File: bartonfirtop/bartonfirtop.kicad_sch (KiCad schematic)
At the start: 23 parts, among them J1 12v Supply, J10 LED8, J11 LED9, J12 LED10, J13 LED11, J14 LED12, J15 LED13, J16 LED14, J17 LED15, J18 LED16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

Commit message: I got a sequence working
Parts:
- added R1: 10k, symbol Device:R
- J19: symbol Connector:Conn_01x03_Pin -> Connector:Conn_01x02_Pin
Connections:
- net GND: no longer J19.2 (Pin_2)
- net at J19.1 (Pin_1), U4.19 (D34): now also R1.2
- net at U4.20 (D35): now also J19.2 (Pin_2); no longer J19.3 (Pin_3)
- net at U1.7 (VCC), U4.1 (3v3): now also R1.1
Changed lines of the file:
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@@
+	)
+	(junction
+		(at 167.64 204.47)
+		(diameter 0)
+		(color 0 0 0 0)
 	)
 	(junction
@@
 	)
 	(junction
+		(at 167.64 67.31)
+		(diameter 0)
+		(color 0 0 0 0)
+	)
+	(junction
 		(at 267.97 87.63)
 		(diameter 0)
@@
 	(wire
 		(pts
-			(xy 256.54 92.71) (xy 246.38 92.71)
+			(xy 255.27 92.71) (xy 246.38 92.71)
 		)
 		(stroke
@@
 	(wire
 		(pts
-			(xy 256.54 208.28) (xy 256.54 92.71)
+			(xy 255.27 207.01) (xy 255.27 92.71)
 		)
 		(stroke
@@
 	(wire
 		(pts
+			(xy 167.64 67.31) (xy 167.64 184.15)
+		)
+		(stroke
+			(width 0)
+			(type default)
+		)
+	)
+	(wire
+		(pts
 			(xy 135.89 158.75) (xy 53.34 158.75)
 		)
@@
 	(wire
 		(pts
+			(xy 167.64 67.31) (xy 133.35 67.31)
+		)
+		(stroke
+			(width 0)
+			(type default)
+		)
+	)
+	(wire
+		(pts
 			(xy 146.05 72.39) (xy 146.05 139.7)
 		)
@@
 	(wire
 		(pts
-			(xy 190.5 208.28) (xy 256.54 208.28)
-		)
-		(stroke
-			(width 0)
-			(type default)
-		)
-	)
-	(wire
-		(pts
 			(xy 278.13 115.57) (xy 267.97 115.57)
 		)
@@
 	(wire
 		(pts
+			(xy 167.64 204.47) (xy 252.73 204.47)
+		)
+		(stroke
+			(width 0)
+			(type default)
+		)
+	)
+	(wire
+		(pts
 			(xy 135.89 113.03) (xy 124.46 113.03)
 		)
@@
 	(wire
 		(pts
-			(xy 190.5 205.74) (xy 267.97 205.74)
-		)
-		(stroke
-			(width 0)
-			(type default)
-		)
-	)
-	(wire
-		(pts
 			(xy 278.13 181.61) (xy 194.31 181.61)
 		)
@@
 	(wire
 		(pts
+			(xy 167.64 191.77) (xy 167.64 204.47)
+		)
+		(stroke
+			(width 0)
+			(type default)
+		)
+	)
+	(wire
+		(pts
 			(xy 127 55.88) (xy 205.74 55.88)
 		)
@@
 	(wire
 		(pts
-			(xy 218.44 67.31) (xy 133.35 67.31)
+			(xy 218.44 67.31) (xy 167.64 67.31)
 		)
 		(stroke
@@
 	(wire
 		(pts
-			(xy 190.5 203.2) (xy 252.73 203.2)
+			(xy 148.59 204.47) (xy 167.64 204.47)
 		)
 		(stroke
@@
 	(wire
 		(pts
-			(xy 267.97 205.74) (xy 267.97 189.23)
+			(xy 267.97 207.01) (xy 267.97 189.23)
 		)
 		(stroke
@@
 	(wire
 		(pts
+			(xy 148.59 207.01) (xy 255.27 207.01)
+		)
+		(stroke
+			(width 0)
+			(type default)
+		)
+	)
+	(wire
+		(pts
 			(xy 267.97 167.64) (xy 267.97 157.48)
 		)
@@
 	(wire
 		(pts
-			(xy 252.73 203.2) (xy 252.73 95.25)
+			(xy 252.73 204.47) (xy 252.73 95.25)
 		)
 		(stroke
@@
 	)
 	(symbol
-		(lib_id "Connector:Conn_01x03_Pin")
-		(at 185.42 205.74 0)
+		(lib_id "Connector:Conn_01x02_Pin")
+		(at 143.51 204.47 0)
 		(unit 1)
 		(exclude_from_sim no)
@@
 		(fields_autoplaced yes)
 		(property "Reference" "J19"
-			(at 186.055 198.12 0)
+			(at 144.145 199.39 0)
 			(effects
 				(font
@@
 		)
 		(property "Value" "AB Switch"
-			(at 186.055 200.66 0)
+			(at 144.145 201.93 0)
 			(effects
 				(font
@@
 		)
 		(property "Footprint" "Connector_Molex:Molex_KK-254_AE-6410-03A_1x03_P2.54mm_Vertical"
-			(at 185.42 205.74 0)
+			(at 143.51 204.47 0)
 			(effects
 				(font
@@
 		)
 		(property "Datasheet" "~"
-			(at 185.42 205.74 0)
-			(effects
-				(font
-					(size 1.27 1.27)
-				)
-				(hide yes)
-			)
-		)
-		(property "Description" "Generic connector, single row, 01x03, script generated"
-			(at 185.42 205.74 0)
-			(effects
-				(font
-					(size 1.27 1.27)
-				)
-				(hide yes)
-			)
-		)
-		(pin "3"
+			(at 143.51 204.47 0)
+			(effects
+				(font
+					(size 1.27 1.27)
+				)
+				(hide yes)
+			)
+		)
+		(property "Description" "Generic connector, single row, 01x02, script generated"
+			(at 143.51 204.47 0)
+			(effects
+				(font
+					(size 1.27 1.27)
+				)
+				(hide yes)
+			)
 		)
 		(pin "1"
@@
 					(unit 1)
 				)
+			)
+		)
+	)
+	(symbol
+		(lib_id "Device:R")
+		(at 167.64 187.96 0)
+		(unit 1)
+		(exclude_from_sim no)
+		(in_bom yes)
+		(on_board yes)
+		(dnp no)
+		(fields_autoplaced yes)
+		(property "Reference" "R1"
+			(at 170.18 186.6899 0)
+			(effects
+				(font
+					(size 1.27 1.27)
+				)
+				(justify left)
+			)
+		)
+		(property "Value" "10k"
+			(at 170.18 189.2299 0)
+			(effects
+				(font
+					(size 1.27 1.27)
+				)
+				(justify left)
+			)
+		)
+		(property "Footprint" ""
+			(at 165.862 187.96 90)
+			(effects
+				(font
+					(size 1.27 1.27)
+				)
+				(hide yes)
+			)
+		)
+		(property "Datasheet" "~"
+			(at 167.64 187.96 0)
+			(effects
+				(font
+					(size 1.27 1.27)
+				)
+				(hide yes)
+			)
+		)
+		(property "Description" "Resistor"
+			(at 167.64 187.96 0)
+			(effects
+				(font
+					(size 1.27 1.27)
+				)
+				(hide yes)
+			)
+		)
+		(pin "1"
+		)
+		(pin "2"
+		)
+		(instances
+			(project "bartonfirtop"
+				(path "/65a05cb8-989d-4b97-b9f4-4e60970e6e14"
+					(reference "R1")
+					(unit 1)
+				)

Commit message: schematic change
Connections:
- net GND: now also J19.2 (Pin_2)
- net at U4.20 (D35): no longer J19.2 (Pin_2)
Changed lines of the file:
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@@
-	(wire
-		(pts
-			(xy 255.27 92.71) (xy 246.38 92.71)
-		)
-		(stroke
-			(width 0)
-			(type default)
-		)
-	)
 	(wire
 		(pts
@@
 	(wire
 		(pts
-			(xy 255.27 207.01) (xy 255.27 92.71)
-		)
-		(stroke
-			(width 0)
-			(type default)
-		)
-	)
-	(wire
-		(pts
 			(xy 278.13 137.16) (xy 267.97 137.16)
 		)
@@
 	(wire
 		(pts
+			(xy 148.59 207.01) (xy 267.97 207.01)
+		)
+		(stroke
+			(width 0)
+			(type default)
+		)
+	)
+	(wire
+		(pts
 			(xy 267.97 115.57) (xy 267.97 105.41)
 		)
@@
 		)
 		(stroke
-			(width 0)
-			(type default)
-		)
-	)
-	(wire
-		(pts
-			(xy 148.59 207.01) (xy 255.27 207.01)
-		)
-		(stroke

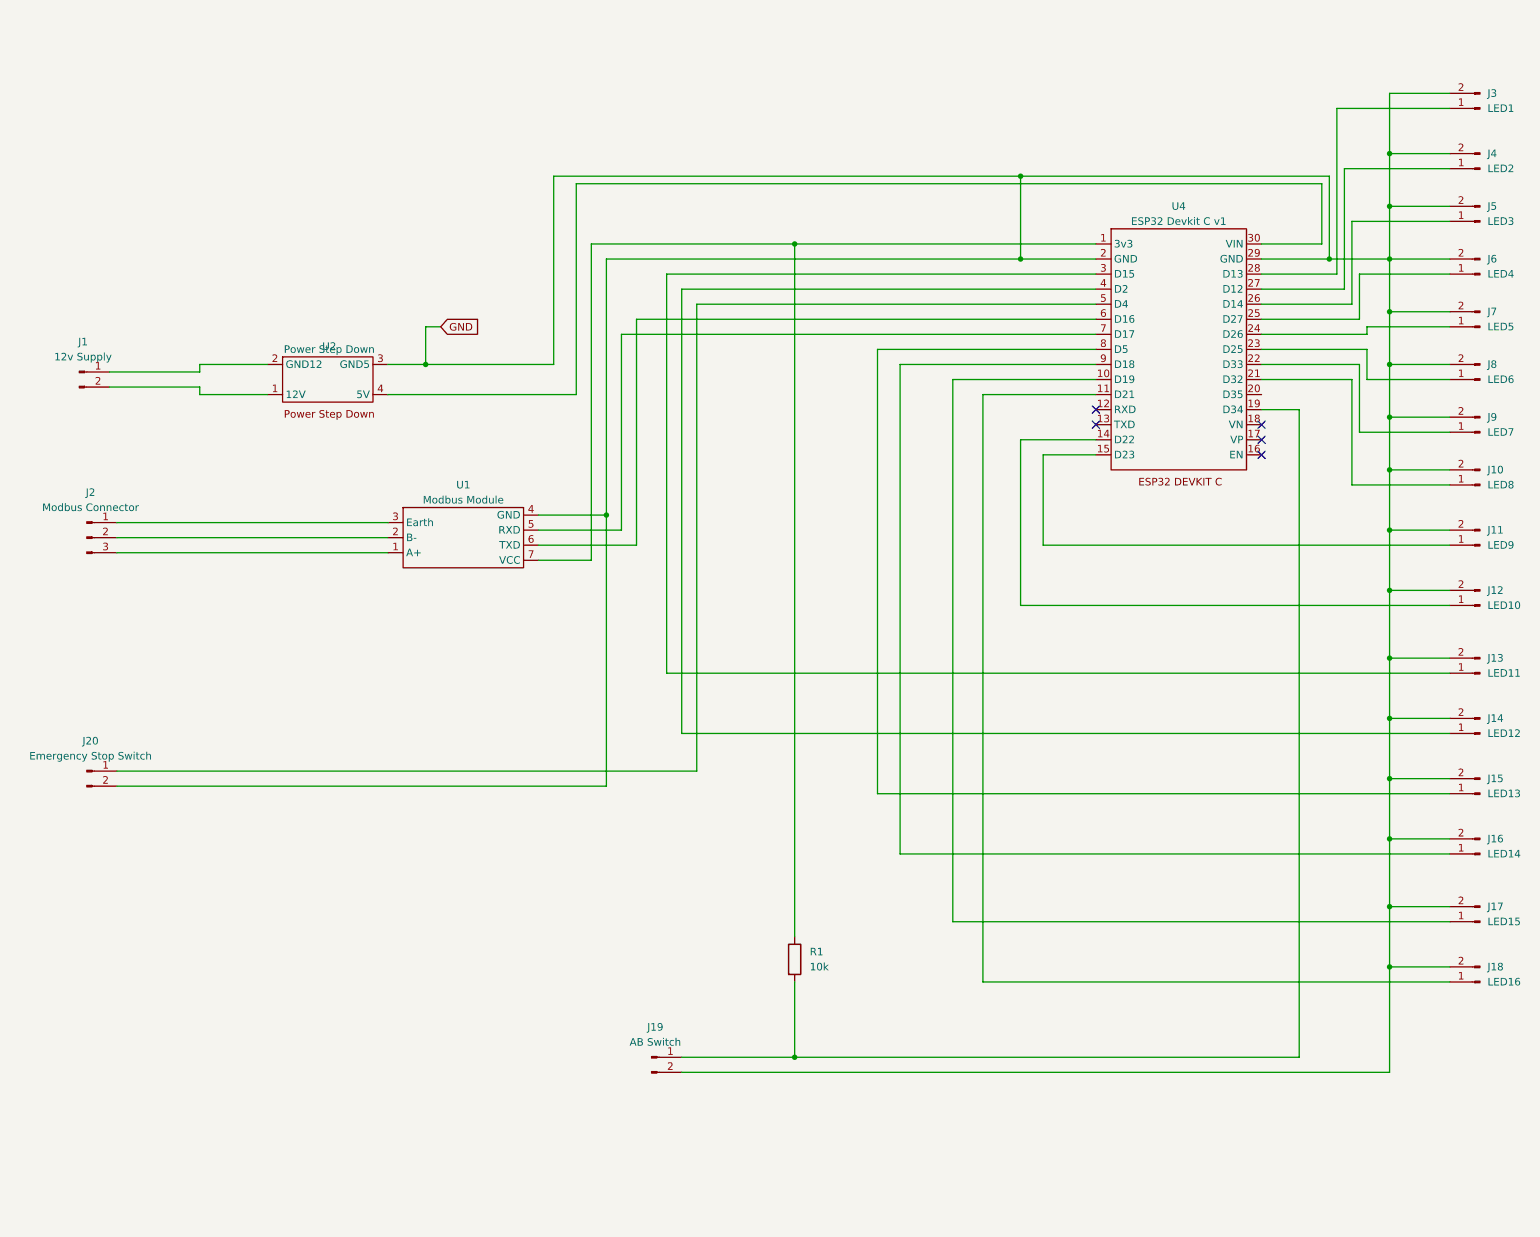
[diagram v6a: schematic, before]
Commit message: added 3 way key switch
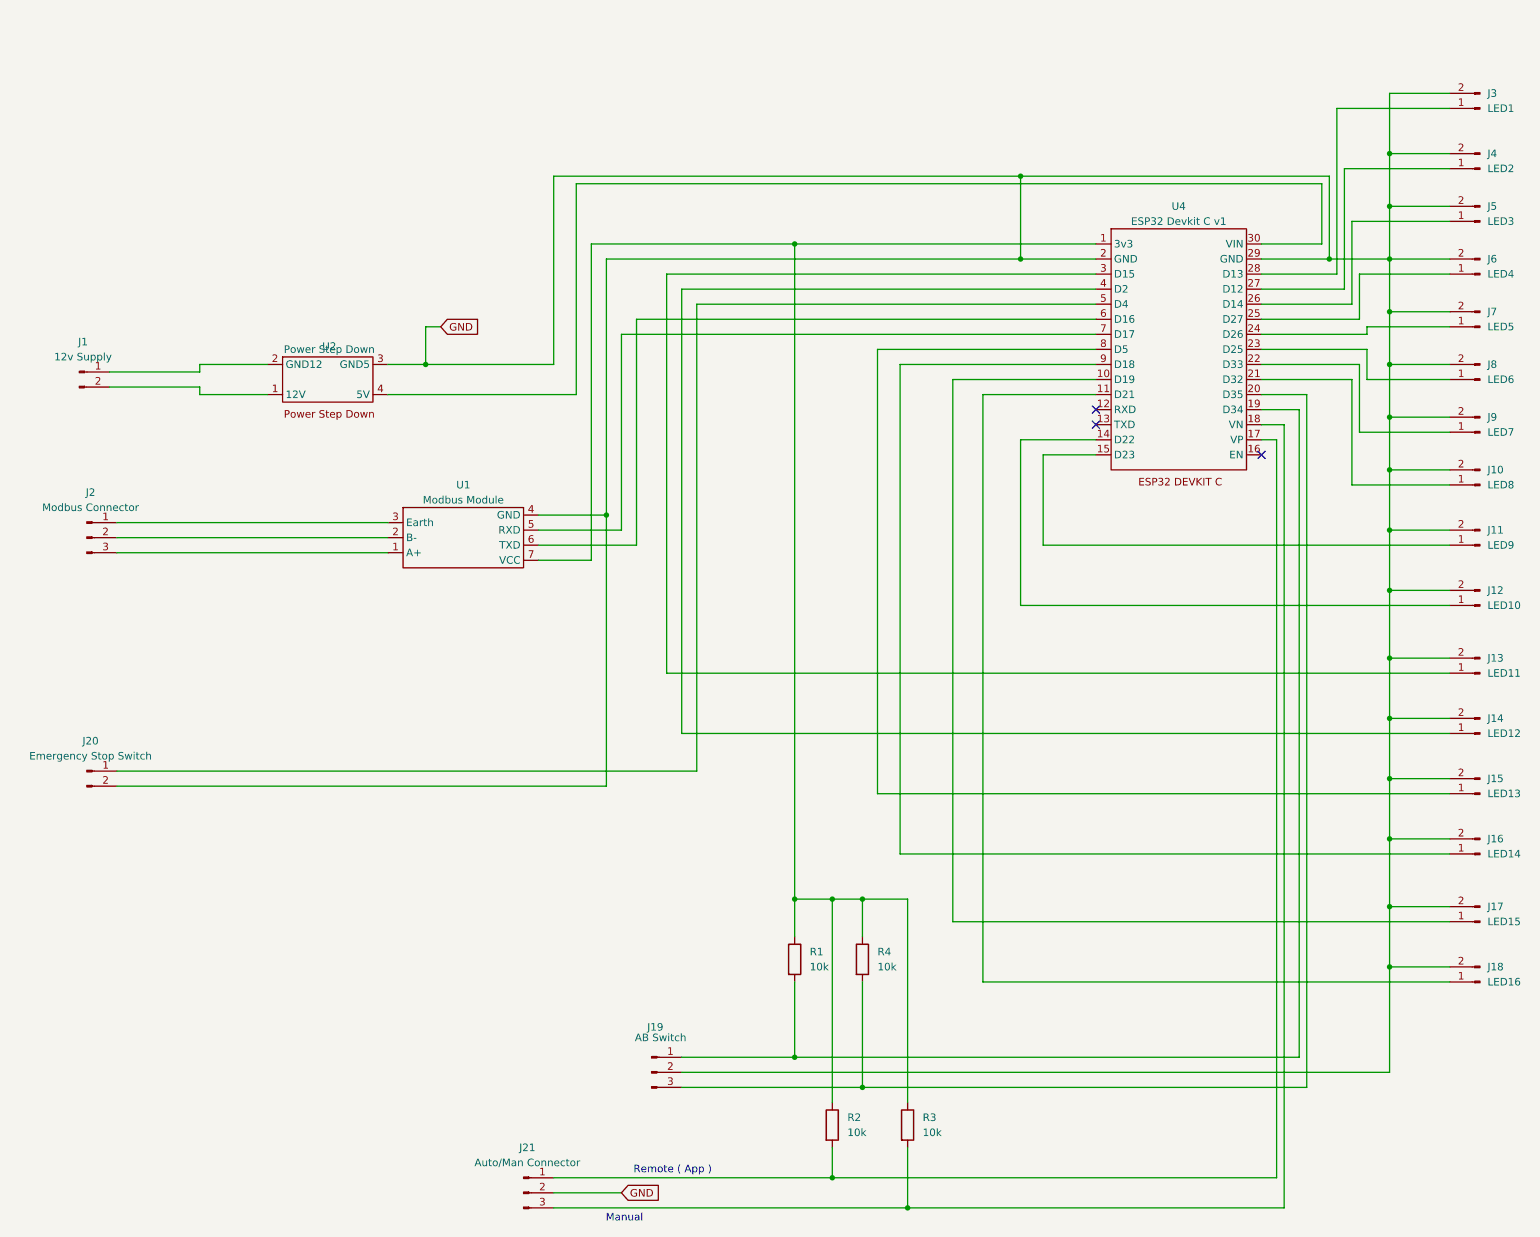
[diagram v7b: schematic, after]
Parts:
- removed J19: AB Switch, Connector_Molex:Molex_KK-254_AE-6410-03A_1x03_P2.54mm_Vertical, symbol Connector:Conn_01x02_Pin
- added J19: AB Switch, Connector_Molex:Molex_KK-254_AE-6410-03A_1x03_P2.54mm_Vertical, symbol Connector:Conn_01x03_Pin
- added J21: Auto/Man Connector, Connector_Molex:Molex_KK-254_AE-6410-03A_1x03_P2.54mm_Vertical, symbol Connector:Conn_01x03_Pin
- added R2, R3, R4: 10k, symbol Device:R
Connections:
- net GND: now also J19.2 (Pin_2), J21.2 (Pin_2)
- net at R1.2, U4.19 (D34): now also J19.1 (Pin_1)
- net at R1.1, U1.7 (VCC), U4.1 (3v3): now also R2.1, R3.1, R4.1
- net at U4.17 (VP): now also J21.1 (Pin_1), R2.2
- net at U4.18 (VN): now also J21.3 (Pin_3), R3.2
- net at U4.20 (D35): now also J19.3 (Pin_3), R4.2
- no-connect marks 5 -> 3
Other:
- note added: "Manual"
- note added: "Remote ( App )"
